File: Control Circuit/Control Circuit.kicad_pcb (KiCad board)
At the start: 2 copper layers, 125.2 x 126 mm, 0 parts

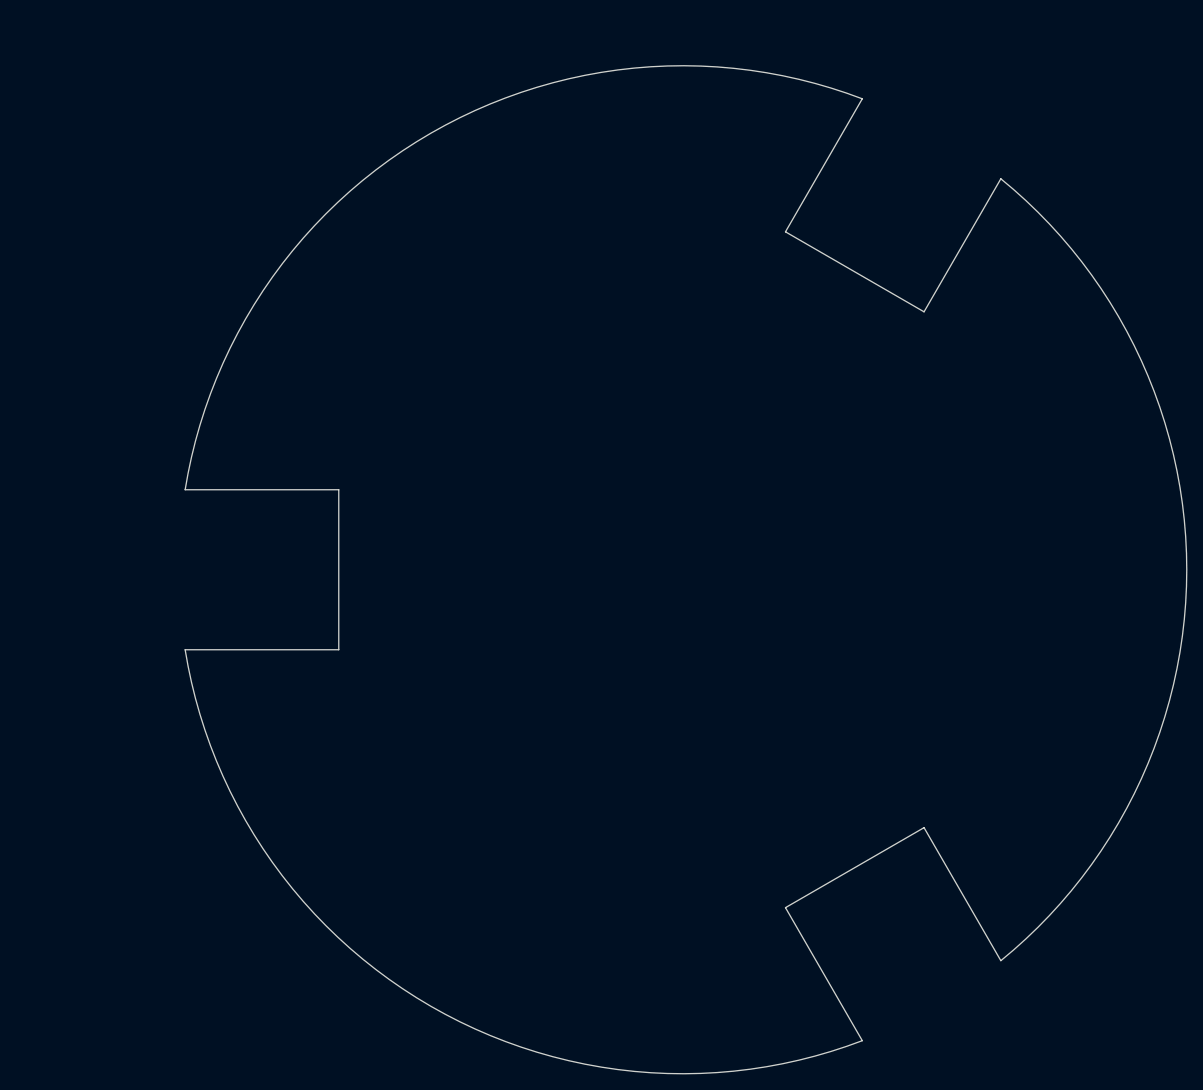
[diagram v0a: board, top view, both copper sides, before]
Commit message: Updated .dxf and control circuit PCB with 3mm tolerance
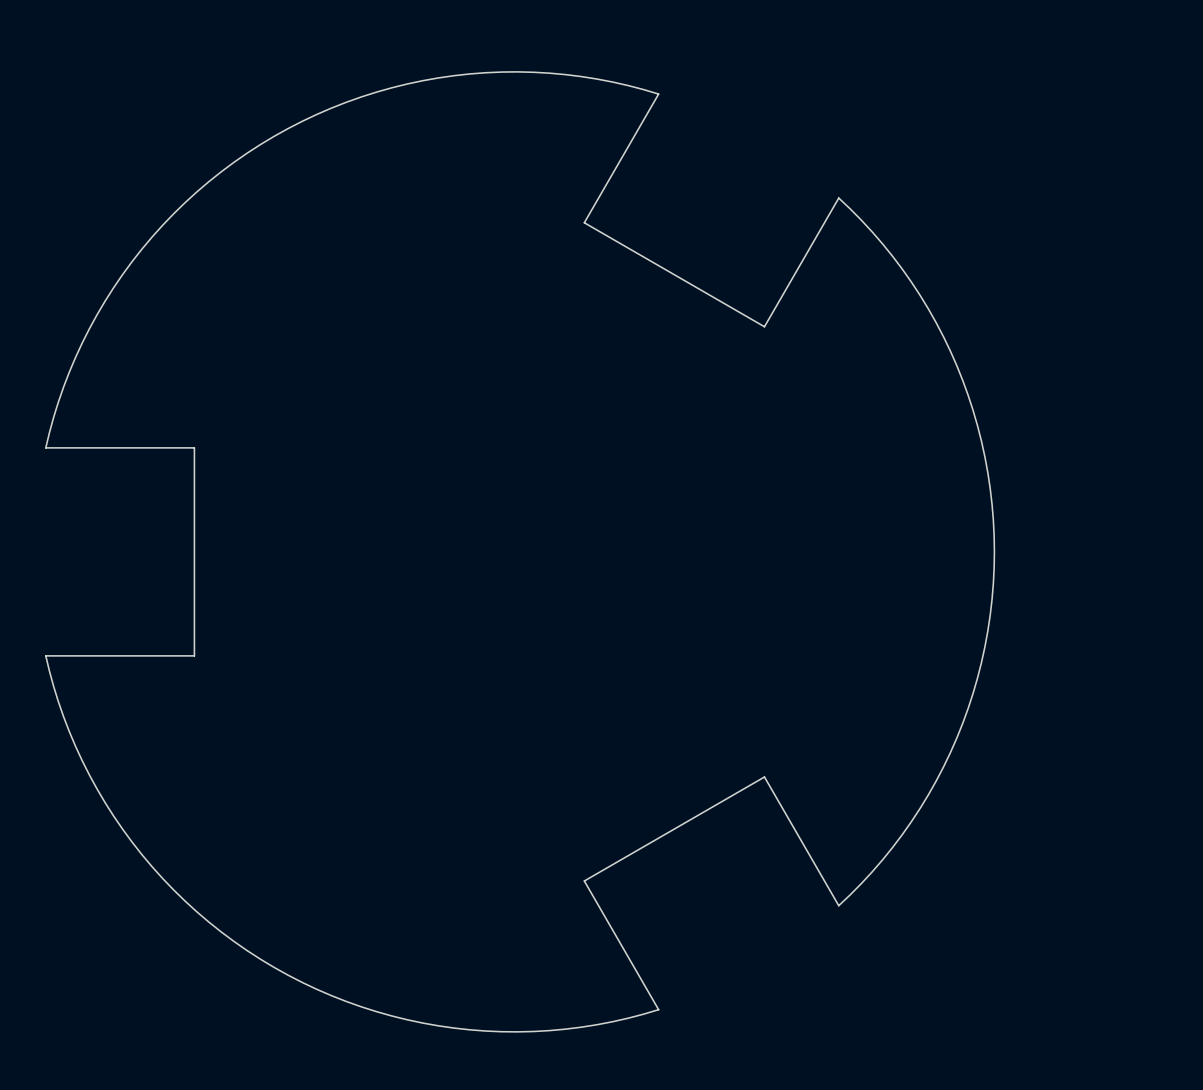
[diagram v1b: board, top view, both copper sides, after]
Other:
- board size 125.2 x 126 mm -> 118.6 x 120 mm
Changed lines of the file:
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@@
   )
   (net 0 "")
-  (gr_line (start 145.79885 58.753014) (end 163.119358 68.753014)
-    (stroke (width 0.1) (type default)) (layer "Edge.Cuts"))
-  (gr_arc (start 70.757819 90.992107) (mid 101.459105 46.432505) (end 155.399493 42.124214)
-    (stroke (width 0.1) (type default)) (layer "Edge.Cuts"))
-  (gr_arc (start 172.72 52.124214) (mid 195.959104 100.992107) (end 172.72 149.86)
-    (stroke (width 0.1) (type default)) (layer "Edge.Cuts"))
-  (gr_line (start 155.399493 159.860001) (end 145.79885 143.2312)
-    (stroke (width 0.1) (type default)) (layer "Edge.Cuts"))
-  (gr_line (start 155.399493 42.124213) (end 145.79885 58.753014)
-    (stroke (width 0.1) (type default)) (layer "Edge.Cuts"))
-  (gr_line (start 145.79885 143.2312) (end 163.119358 133.2312)
-    (stroke (width 0.1) (type default)) (layer "Edge.Cuts"))
-  (gr_line (start 70.757818 90.992107) (end 89.959103 90.992107)
-    (stroke (width 0.1) (type default)) (layer "Edge.Cuts"))
-  (gr_line (start 89.959103 90.992107) (end 89.959103 110.992107)
-    (stroke (width 0.1) (type default)) (layer "Edge.Cuts"))
-  (gr_line (start 89.959103 110.992107) (end 70.757818 110.992107)
-    (stroke (width 0.1) (type default)) (layer "Edge.Cuts"))
-  (gr_line (start 163.119358 133.2312) (end 172.720001 149.860001)
-    (stroke (width 0.1) (type default)) (layer "Edge.Cuts"))
-  (gr_line (start 172.72 52.124214) (end 163.119358 68.753014)
-    (stroke (width 0.1) (type default)) (layer "Edge.Cuts"))
-  (gr_arc (start 155.399493 159.86) (mid 101.459107 155.551704) (end 70.757819 110.992107)
-    (stroke (width 0.1) (type default)) (layer "Edge.Cuts"))
+  (gr_line (start 143.17307 126.901017) (end 120.656409 139.901017)
+    (stroke (width 0.2) (type solid)) (layer "Edge.Cuts"))
+  (gr_line (start 53.34 111.76) (end 71.914738 111.76)
+    (stroke (width 0.2) (type solid)) (layer "Edge.Cuts"))
+  (gr_line (start 71.914738 111.76) (end 71.914738 85.76)
+    (stroke (width 0.2) (type solid)) (layer "Edge.Cuts"))
+  (gr_line (start 152.460439 142.987212) (end 143.17307 126.901017)
+    (stroke (width 0.2) (type solid)) (layer "Edge.Cuts"))
+  (gr_line (start 143.17307 70.618983) (end 152.460439 54.532788)
+    (stroke (width 0.2) (type solid)) (layer "Edge.Cuts"))
+  (gr_arc (start 129.943778 155.987212) (mid 81.914739 150.721524) (end 53.34 111.76)
+    (stroke (width 0.2) (type solid)) (layer "Edge.Cuts"))
+  (gr_line (start 120.656409 57.618983) (end 143.17307 70.618983)
+    (stroke (width 0.2) (type solid)) (layer "Edge.Cuts"))
+  (gr_arc (start 53.34 85.76) (mid 81.914739 46.798476) (end 129.943778 41.532788)
+    (stroke (width 0.2) (type solid)) (layer "Edge.Cuts"))
+  (gr_arc (start 152.460439 54.532788) (mid 171.914739 98.76) (end 152.460439 142.987212)
+    (stroke (width 0.2) (type solid)) (layer "Edge.Cuts"))
+  (gr_line (start 129.943778 41.532788) (end 120.656409 57.618983)
+    (stroke (width 0.2) (type solid)) (layer "Edge.Cuts"))
+  (gr_line (start 71.914738 85.76) (end 53.34 85.76)
+    (stroke (width 0.2) (type solid)) (layer "Edge.Cuts"))
+  (gr_line (start 120.656409 139.901017) (end 129.943778 155.987212)
+    (stroke (width 0.2) (type solid)) (layer "Edge.Cuts"))
+  (group "" (id d9ff58da-d626-4267-b94a-bc169973c5e5)
+    (members
+      03e5a22f-747a-4755-b2d9-5b0fd53b9463
+      1bf3ae57-108e-432e-935b-dc585a51e9f2
+      1cff9b36-c665-4a7f-8d07-4fa604743f36
+      3126e0ea-1537-4ed2-8ee2-12426cb289b1
+      41f21fc9-91e7-424a-b463-4139455cccdd
+      b1c2d789-4e2b-4df5-a4ae-ac27cbc04bc7
+      baa51c8c-5b4c-489d-906b-d9b7b1bd2978
+      d7bb7529-d266-475d-9266-311995f215a5
+      df1be2f9-9ed0-401a-a2f8-5f0bf1c350b6
+      e0b4e479-4ccb-408d-ad39-4ea0b5519bc5
+      ea232489-3607-4806-962b-fc4ea7b62cc3
+      f7ef9afd-121d-4120-856b-5c997b0fda9b
+    )
+  )
 )

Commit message: Added symbol and footprint for baro and IMU
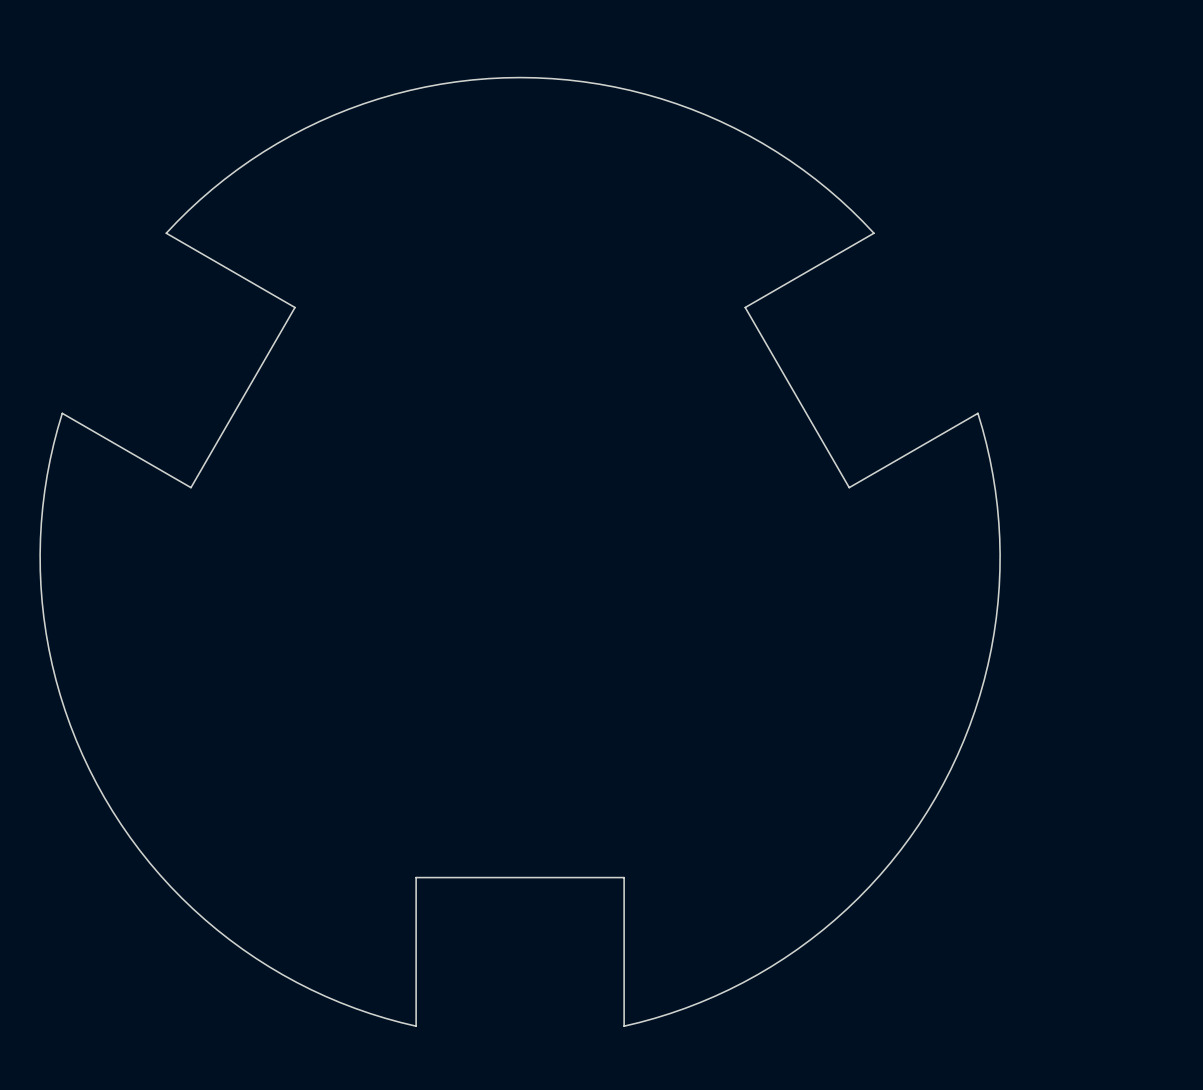
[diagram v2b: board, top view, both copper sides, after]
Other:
- board size 118.6 x 120 mm -> 120 x 118.6 mm
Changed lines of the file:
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@@
   )
   (net 0 "")
-  (gr_line (start 143.17307 126.901017) (end 120.656409 139.901017)
+  (gr_line (start 140.768388 68.214299) (end 153.768388 90.73096)
     (stroke (width 0.2) (type solid)) (layer "Edge.Cuts"))
-  (gr_line (start 53.34 111.76) (end 71.914738 111.76)
+  (gr_line (start 125.627371 158.047369) (end 125.627371 139.472631)
     (stroke (width 0.2) (type solid)) (layer "Edge.Cuts"))
-  (gr_line (start 71.914738 111.76) (end 71.914738 85.76)
+  (gr_line (start 125.627371 139.472631) (end 99.627371 139.472631)
     (stroke (width 0.2) (type solid)) (layer "Edge.Cuts"))
-  (gr_line (start 152.460439 142.987212) (end 143.17307 126.901017)
+  (gr_line (start 156.854583 58.92693) (end 140.768388 68.214299)
     (stroke (width 0.2) (type solid)) (layer "Edge.Cuts"))
-  (gr_line (start 143.17307 70.618983) (end 152.460439 54.532788)
+  (gr_line (start 84.486354 68.214299) (end 68.400159 58.92693)
     (stroke (width 0.2) (type solid)) (layer "Edge.Cuts"))
-  (gr_arc (start 129.943778 155.987212) (mid 81.914739 150.721524) (end 53.34 111.76)
+  (gr_arc (start 169.854583 81.443591) (mid 164.588895 129.47263) (end 125.627371 158.047369)
     (stroke (width 0.2) (type solid)) (layer "Edge.Cuts"))
-  (gr_line (start 120.656409 57.618983) (end 143.17307 70.618983)
+  (gr_line (start 71.486354 90.73096) (end 84.486354 68.214299)
     (stroke (width 0.2) (type solid)) (layer "Edge.Cuts"))
-  (gr_arc (start 53.34 85.76) (mid 81.914739 46.798476) (end 129.943778 41.532788)
+  (gr_arc (start 99.627371 158.047369) (mid 60.665846 129.47263) (end 55.400159 81.443591)
     (stroke (width 0.2) (type solid)) (layer "Edge.Cuts"))
-  (gr_arc (start 152.460439 54.532788) (mid 171.914739 98.76) (end 152.460439 142.987212)
+  (gr_arc (start 68.400159 58.92693) (mid 112.627371 39.472629) (end 156.854583 58.92693)
     (stroke (width 0.2) (type solid)) (layer "Edge.Cuts"))
-  (gr_line (start 129.943778 41.532788) (end 120.656409 57.618983)
+  (gr_line (start 55.400159 81.443591) (end 71.486354 90.73096)
     (stroke (width 0.2) (type solid)) (layer "Edge.Cuts"))
-  (gr_line (start 71.914738 85.76) (end 53.34 85.76)
+  (gr_line (start 99.627371 139.472631) (end 99.627371 158.047369)
     (stroke (width 0.2) (type solid)) (layer "Edge.Cuts"))
-  (gr_line (start 120.656409 139.901017) (end 129.943778 155.987212)
+  (gr_line (start 153.768388 90.73096) (end 169.854583 81.443591)
     (stroke (width 0.2) (type solid)) (layer "Edge.Cuts"))
   (group "" (id d9ff58da-d626-4267-b94a-bc169973c5e5)

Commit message: fixed .step file not loading
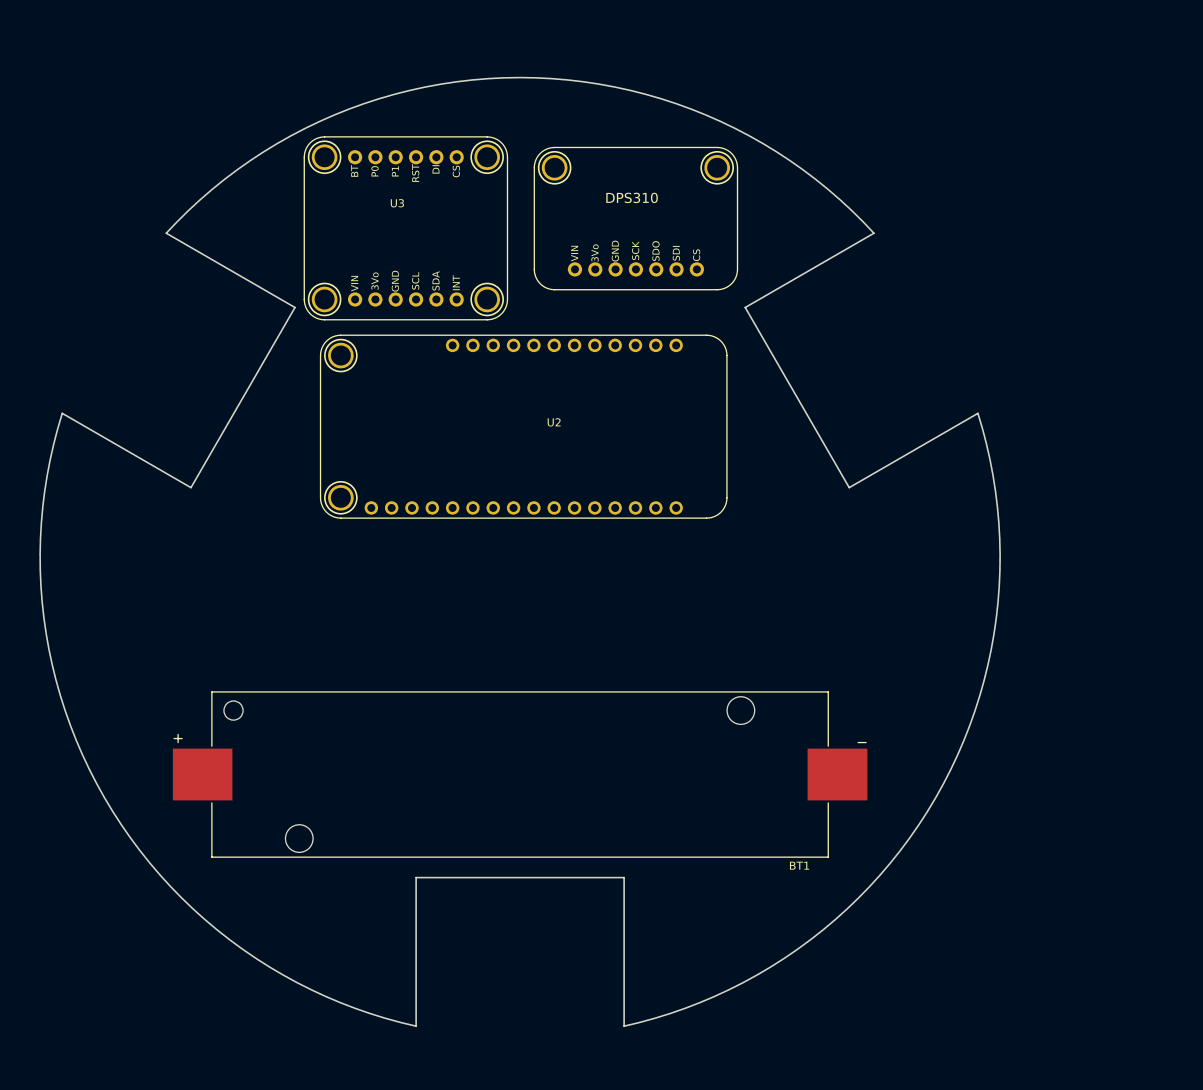
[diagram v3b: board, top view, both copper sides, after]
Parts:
- added BT1: 18650 Cell holder, 18650 Cell Holder:18560 holder, F.Cu at (112.6, 126.6)
- added U1: Adafruit DPS310, DPS310:Adafruit DPS310, F.Cu at (126.6, 55.1)
- added U2: ~, STM32F405:Adafruit Feather STM32F405 Express, F.Cu at (116.9, 83.1)
- added U3: Adafruit BNO085, BNO085:Adafruit BNO085, F.Cu at (97.8, 57.0)
